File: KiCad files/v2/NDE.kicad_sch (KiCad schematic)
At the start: 11 parts, among them J1 Nabíjací modul, J2 Step-up input, J3 Step-up output, U1 LM7805_TO220

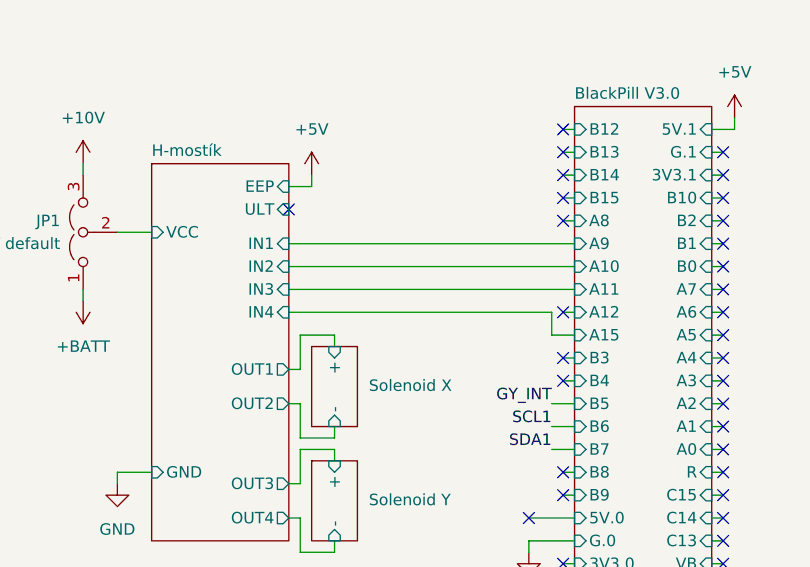
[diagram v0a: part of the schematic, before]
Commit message: Improved routing and layout
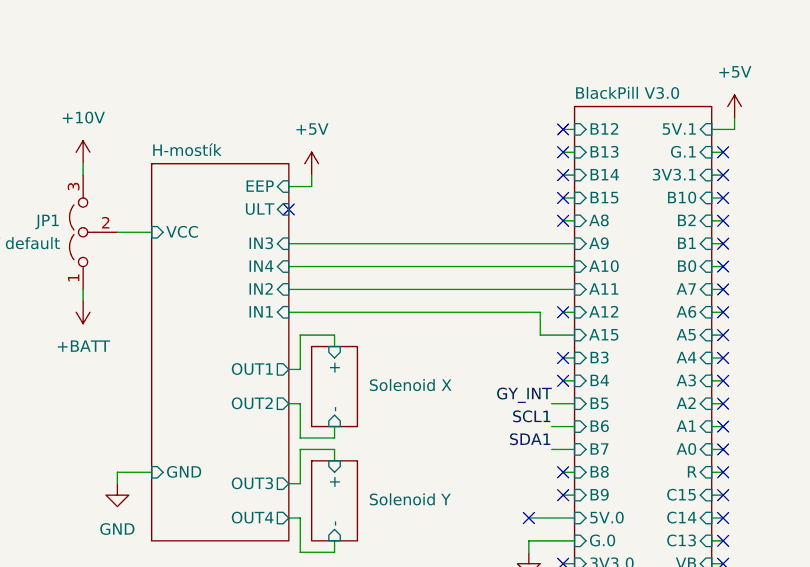
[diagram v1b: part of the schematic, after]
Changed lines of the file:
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@@
 	(wire
 		(pts
+			(xy 109.22 91.44) (xy 140.97 91.44)
+		)
+		(stroke
+			(width 0)
+			(type default)
+		)
+	)
+	(wire
+		(pts
 			(xy 110.49 118.11) (xy 110.49 114.3)
 		)
@@
 	(wire
 		(pts
-			(xy 109.22 93.98) (xy 140.97 93.98)
-		)
-		(stroke
-			(width 0)
-			(type default)
-		)
-	)
-	(wire
-		(pts
 			(xy 86.36 96.52) (xy 86.36 97.79)
 		)
@@
 	(wire
 		(pts
-			(xy 109.22 96.52) (xy 140.97 96.52)
-		)
-		(stroke
-			(width 0)
-			(type default)
-		)
-	)
-	(wire
-		(pts
 			(xy 208.28 87.63) (xy 212.09 87.63)
 		)
@@
 	(wire
 		(pts
-			(xy 138.43 99.06) (xy 138.43 101.6)
-		)
-		(stroke
-			(width 0)
-			(type default)
-		)
-	)
-	(wire
-		(pts
 			(xy 156.21 93.98) (xy 157.48 93.98)
 		)
@@
 	(wire
 		(pts
+			(xy 109.22 99.06) (xy 137.16 99.06)
+		)
+		(stroke
+			(width 0)
+			(type default)
+		)
+	)
+	(wire
+		(pts
 			(xy 212.09 119.38) (xy 212.09 118.11)
 		)
@@
 	(wire
 		(pts
-			(xy 109.22 91.44) (xy 140.97 91.44)
+			(xy 156.21 116.84) (xy 157.48 116.84)
 		)
 		(stroke
@@
 	(wire
 		(pts
-			(xy 156.21 116.84) (xy 157.48 116.84)
+			(xy 43.18 97.79) (xy 35.56 97.79)
 		)
 		(stroke
@@
 	(wire
 		(pts
-			(xy 43.18 97.79) (xy 35.56 97.79)
+			(xy 179.07 29.21) (xy 179.07 34.29)
 		)
 		(stroke
@@
 	(wire
 		(pts
-			(xy 179.07 29.21) (xy 179.07 34.29)
+			(xy 137.16 101.6) (xy 140.97 101.6)
 		)
 		(stroke
@@
 	(wire
 		(pts
+			(xy 137.16 99.06) (xy 137.16 101.6)
+		)
+		(stroke
+			(width 0)
+			(type default)
+		)
+	)
+	(wire
+		(pts
 			(xy 156.21 86.36) (xy 157.48 86.36)
 		)
@@
 	(wire
 		(pts
-			(xy 213.36 134.62) (xy 212.09 134.62)
+			(xy 109.22 93.98) (xy 140.97 93.98)
 		)
 		(stroke
@@
 	(wire
 		(pts
-			(xy 148.59 29.21) (xy 148.59 34.29)
+			(xy 213.36 134.62) (xy 212.09 134.62)
 		)
 		(stroke
@@
 	(wire
 		(pts
-			(xy 138.43 114.3) (xy 140.97 114.3)
+			(xy 148.59 29.21) (xy 148.59 34.29)
 		)
 		(stroke
@@
 	(wire
 		(pts
-			(xy 43.18 116.84) (xy 43.18 118.11)
+			(xy 138.43 114.3) (xy 140.97 114.3)
 		)
 		(stroke
@@
 	(wire
 		(pts
-			(xy 156.21 111.76) (xy 157.48 111.76)
+			(xy 43.18 116.84) (xy 43.18 118.11)
 		)
 		(stroke
@@
 	(wire
 		(pts
-			(xy 90.17 116.84) (xy 90.17 118.11)
+			(xy 156.21 111.76) (xy 157.48 111.76)
 		)
 		(stroke
@@
 	(wire
 		(pts
-			(xy 156.21 81.28) (xy 157.48 81.28)
+			(xy 90.17 116.84) (xy 90.17 118.11)
 		)
 		(stroke
@@
 	(wire
 		(pts
-			(xy 109.22 118.11) (xy 110.49 118.11)
+			(xy 156.21 81.28) (xy 157.48 81.28)
 		)
 		(stroke
@@
 	(wire
 		(pts
-			(xy 138.43 101.6) (xy 140.97 101.6)
+			(xy 109.22 96.52) (xy 140.97 96.52)
 		)
 		(stroke
@@
 	(wire
 		(pts
-			(xy 43.18 101.6) (xy 43.18 100.33)
+			(xy 109.22 118.11) (xy 110.49 118.11)
 		)
 		(stroke
@@
 	(wire
 		(pts
-			(xy 109.22 99.06) (xy 138.43 99.06)
+			(xy 43.18 101.6) (xy 43.18 100.33)
 		)
 		(stroke
@@
 		)
 		(pin "IN1" input
-			(at 109.22 91.44 0)
+			(at 109.22 99.06 0)
 			(effects
 				(font
@@
 		)
 		(pin "IN2" input
-			(at 109.22 93.98 0)
+			(at 109.22 96.52 0)
 			(effects
 				(font
@@
 		)
 		(pin "IN3" input
-			(at 109.22 96.52 0)
+			(at 109.22 91.44 0)
 			(effects
 				(font
@@
 		)
 		(pin "IN4" input
-			(at 109.22 99.06 0)
+			(at 109.22 93.98 0)
 			(effects
 				(font

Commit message: v2 ready for manufacturing
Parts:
- added H1, H2, H3, H4, H5, H6: MountingHole, MountingHole:MountingHole_3.2mm_M3_ISO14580, symbol Mechanical:MountingHole
